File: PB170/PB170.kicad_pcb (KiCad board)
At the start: 4 copper layers, 96.5 x 71.1 mm, 34 parts, among them J1 USB_C_Receptacle_USB2.0-Conne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, J2 USB_B_Micro, Q1 P-MOSFET-MLP_HS, Q2 BC817, SW1 SW_MEC_5E, SW2 SW_MEC_5E, U1 74HC00

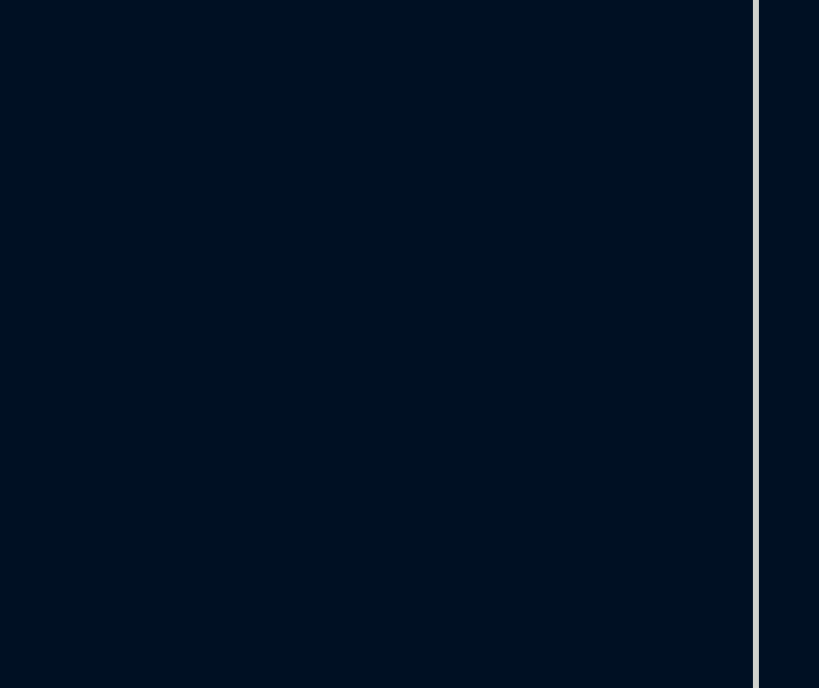
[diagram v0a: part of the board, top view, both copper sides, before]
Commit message: Experimentally added 74HC08 symbol.
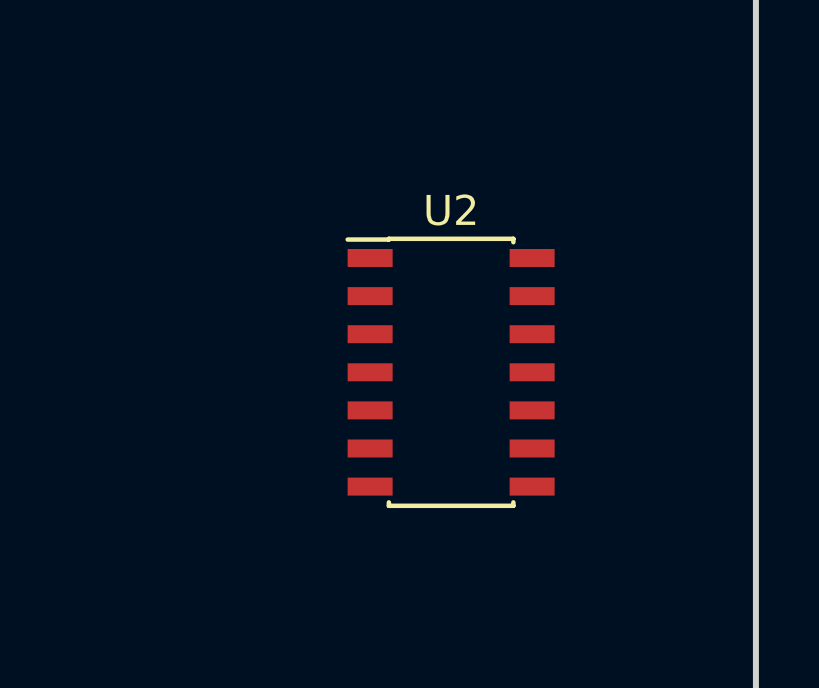
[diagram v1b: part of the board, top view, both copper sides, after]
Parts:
- added U2: 74HC08, Housings_SOIC:SOIC-14_3.9x8.7mm_Pitch1.27mm, F.Cu at (127.0, 48.5)
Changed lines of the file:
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@@
     (tracks 30)
     (zones 0)
-    (modules 34)
-    (nets 32)
+    (modules 35)
+    (nets 44)
   )
   (page A4)
@@
   (net 30 /SheetXOR/IN_B)
   (net 31 OUTPUT)
+  (net 32 "Net-(U2-Pad1)")
+  (net 33 "Net-(U2-Pad2)")
+  (net 34 "Net-(U2-Pad4)")
+  (net 35 "Net-(U2-Pad6)")
+  (net 36 "Net-(U2-Pad8)")
+  (net 37 "Net-(U2-Pad9)")
+  (net 38 "Net-(U2-Pad10)")
+  (net 39 "Net-(U2-Pad11)")
+  (net 40 "Net-(U2-Pad12)")
+  (net 41 "Net-(U2-Pad13)")
+  (net 42 "Net-(U2-Pad3)")
+  (net 43 "Net-(U2-Pad5)")
   (net_class Default "This is the default net class."
     (clearance 0.2)
@@
     (add_net "Net-(U1-Pad13)")
     (add_net "Net-(U1-Pad3)")
+    (add_net "Net-(U2-Pad1)")
+    (add_net "Net-(U2-Pad10)")
+    (add_net "Net-(U2-Pad11)")
+    (add_net "Net-(U2-Pad12)")
+    (add_net "Net-(U2-Pad13)")
+    (add_net "Net-(U2-Pad2)")
+    (add_net "Net-(U2-Pad3)")
+    (add_net "Net-(U2-Pad4)")
+    (add_net "Net-(U2-Pad5)")
+    (add_net "Net-(U2-Pad6)")
+    (add_net "Net-(U2-Pad8)")
+    (add_net "Net-(U2-Pad9)")
     (add_net OUTPUT)
   )
+  (module Housings_SOIC:SOIC-14_3.9x8.7mm_Pitch1.27mm (layer F.Cu)
+    (at 127 48.514)
+    (descr "14-Lead Plastic Small Outline (SL) - Narrow, 3.90 mm Body [SOIC] (see Microchip Packaging Specification 00000049BS.pdf)")
+    (tags "SOIC 1.27")
+    (attr smd)
+    (fp_text reference U2 (at 0 -5.375) (layer F.SilkS)
+      (effects (font (size 1 1) (thickness 0.15)))
+    )
+    (fp_text value 74HC08 (at 0 5.375) (layer F.Fab)
+      (effects (font (size 1 1) (thickness 0.15)))
+    )
+    (fp_line (start -2.075 -4.425) (end -3.45 -4.425) (layer F.SilkS) (width 0.15))
+    (fp_line (start -2.075 4.45) (end 2.075 4.45) (layer F.SilkS) (width 0.15))
+    (fp_line (start -2.075 -4.45) (end 2.075 -4.45) (layer F.SilkS) (width 0.15))
+    (fp_line (start -2.075 4.45) (end -2.075 4.335) (layer F.SilkS) (width 0.15))
+    (fp_line (start 2.075 4.45) (end 2.075 4.335) (layer F.SilkS) (width 0.15))
+    (fp_line (start 2.075 -4.45) (end 2.075 -4.335) (layer F.SilkS) (width 0.15))
+    (fp_line (start -2.075 -4.45) (end -2.075 -4.425) (layer F.SilkS) (width 0.15))
+    (fp_line (start -3.7 4.65) (end 3.7 4.65) (layer F.CrtYd) (width 0.05))
+    (fp_line (start -3.7 -4.65) (end 3.7 -4.65) (layer F.CrtYd) (width 0.05))
+    (fp_line (start 3.7 -4.65) (end 3.7 4.65) (layer F.CrtYd) (width 0.05))
+    (fp_line (start -3.7 -4.65) (end -3.7 4.65) (layer F.CrtYd) (width 0.05))
+    (fp_line (start -1.95 -3.35) (end -0.95 -4.35) (layer F.Fab) (width 0.15))
+    (fp_line (start -1.95 4.35) (end -1.95 -3.35) (layer F.Fab) (width 0.15))
+    (fp_line (start 1.95 4.35) (end -1.95 4.35) (layer F.Fab) (width 0.15))
+    (fp_line (start 1.95 -4.35) (end 1.95 4.35) (layer F.Fab) (width 0.15))
+    (fp_line (start -0.95 -4.35) (end 1.95 -4.35) (layer F.Fab) (width 0.15))
+    (fp_text user %R (at 0 0) (layer F.Fab)
+      (effects (font (size 0.9 0.9) (thickness 0.135)))
+    )
+    (pad 1 smd rect (at -2.7 -3.81) (size 1.5 0.6) (layers F.Cu F.Paste F.Mask)
+      (net 32 "Net-(U2-Pad1)"))
+    (pad 2 smd rect (at -2.7 -2.54) (size 1.5 0.6) (layers F.Cu F.Paste F.Mask)
+      (net 33 "Net-(U2-Pad2)"))
+    (pad 3 smd rect (at -2.7 -1.27) (size 1.5 0.6) (layers F.Cu F.Paste F.Mask)
+      (net 42 "Net-(U2-Pad3)"))
+    (pad 4 smd rect (at -2.7 0) (size 1.5 0.6) (layers F.Cu F.Paste F.Mask)
+      (net 34 "Net-(U2-Pad4)"))
+    (pad 5 smd rect (at -2.7 1.27) (size 1.5 0.6) (layers F.Cu F.Paste F.Mask)
+      (net 43 "Net-(U2-Pad5)"))
+    (pad 6 smd rect (at -2.7 2.54) (size 1.5 0.6) (layers F.Cu F.Paste F.Mask)
+      (net 35 "Net-(U2-Pad6)"))
+    (pad 7 smd rect (at -2.7 3.81) (size 1.5 0.6) (layers F.Cu F.Paste F.Mask)
+      (net 3 GND))
+    (pad 8 smd rect (at 2.7 3.81) (size 1.5 0.6) (layers F.Cu F.Paste F.Mask)
+      (net 36 "Net-(U2-Pad8)"))
+    (pad 9 smd rect (at 2.7 2.54) (size 1.5 0.6) (layers F.Cu F.Paste F.Mask)
+      (net 37 "Net-(U2-Pad9)"))
+    (pad 10 smd rect (at 2.7 1.27) (size 1.5 0.6) (layers F.Cu F.Paste F.Mask)
+      (net 38 "Net-(U2-Pad10)"))
+    (pad 11 smd rect (at 2.7 0) (size 1.5 0.6) (layers F.Cu F.Paste F.Mask)
+      (net 39 "Net-(U2-Pad11)"))
+    (pad 12 smd rect (at 2.7 -1.27) (size 1.5 0.6) (layers F.Cu F.Paste F.Mask)
+      (net 40 "Net-(U2-Pad12)"))
+    (pad 13 smd rect (at 2.7 -2.54) (size 1.5 0.6) (layers F.Cu F.Paste F.Mask)
+      (net 41 "Net-(U2-Pad13)"))
+    (pad 14 smd rect (at 2.7 -3.81) (size 1.5 0.6) (layers F.Cu F.Paste F.Mask)
+      (net 2 +5V))
+    (model ${KISYS3DMOD}/Housings_SOIC.3dshapes/SOIC-14_3.9x8.7mm_Pitch1.27mm.wrl
+      (at (xyz 0 0 0))
+      (scale (xyz 1 1 1))
+      (rotate (xyz 0 0 0))
+    )
+  )
   (module Resistors_SMD:R_0603 (layer F.Cu)

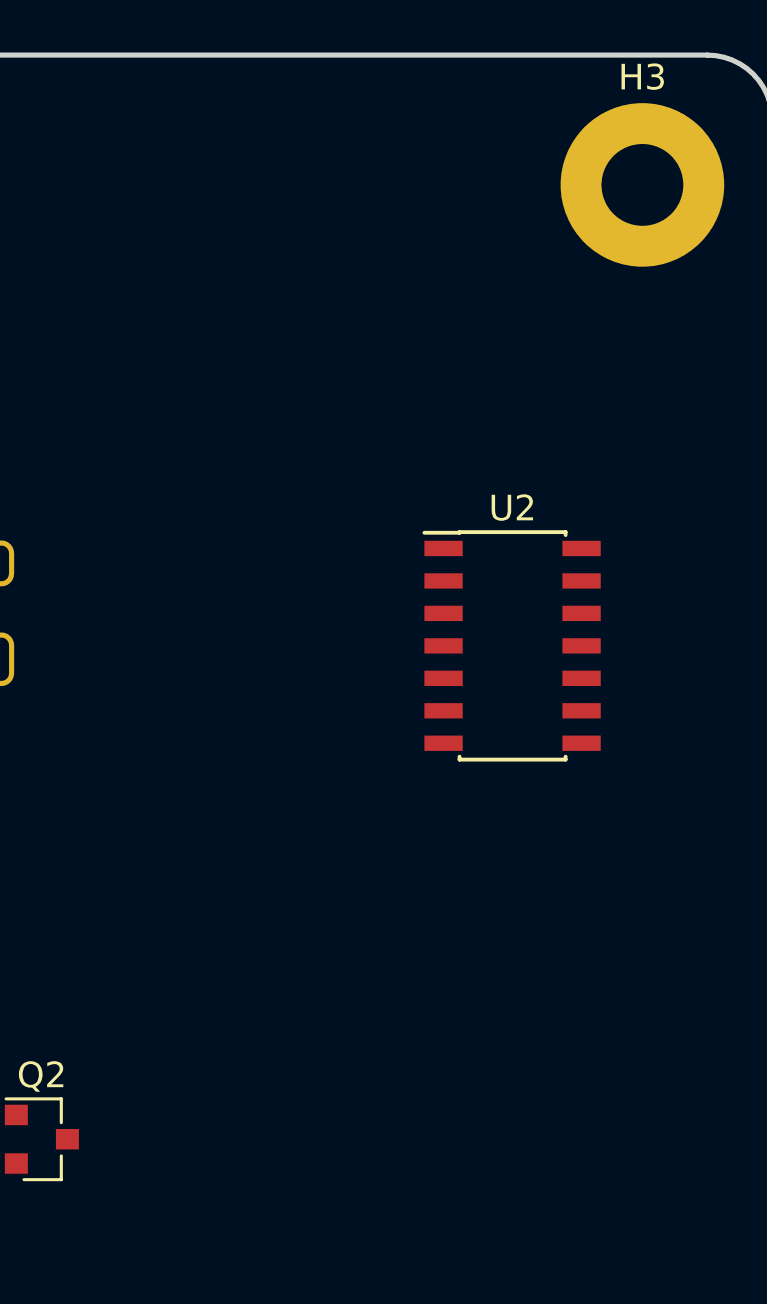
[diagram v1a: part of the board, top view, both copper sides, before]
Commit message: Added 74HC4511D and HEF4518BT.
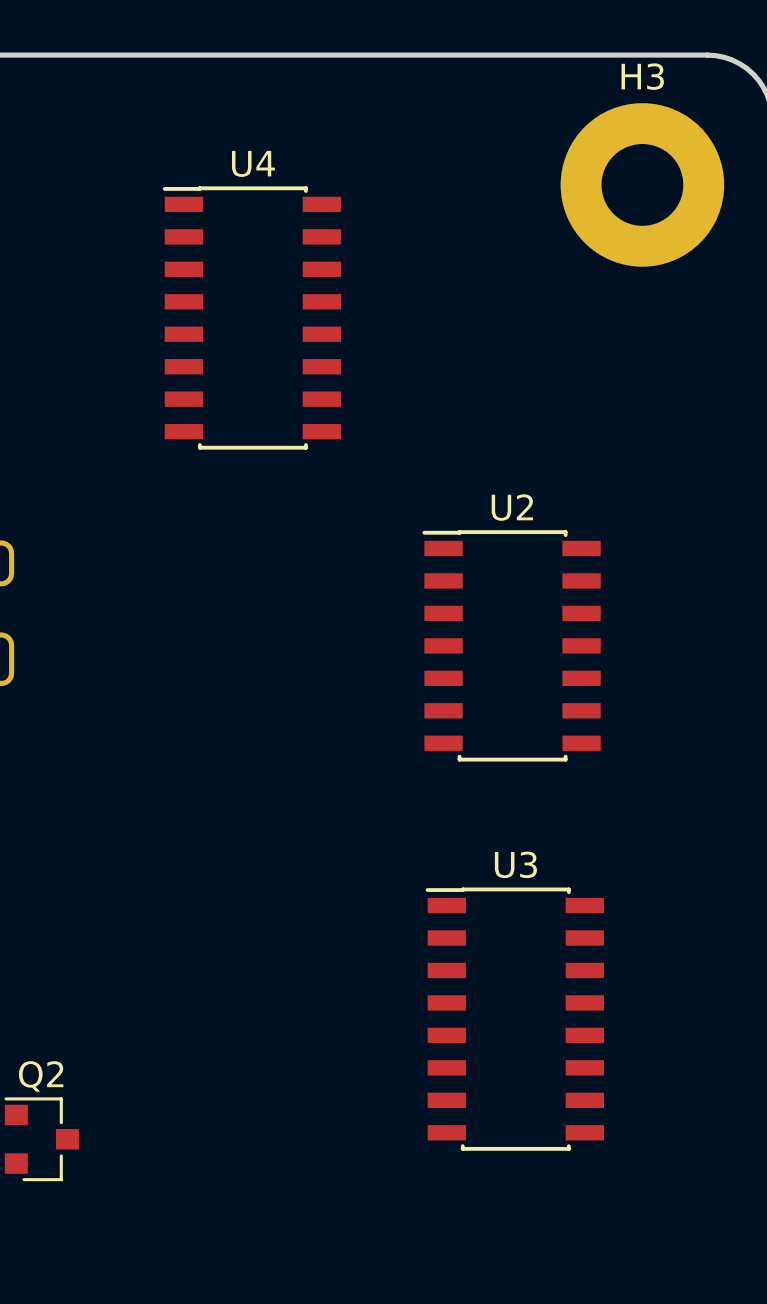
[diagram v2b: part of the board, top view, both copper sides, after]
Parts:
- added U3: 74HC4511D, Housings_SOIC:SOIC-16_3.9x9.9mm_Pitch1.27mm, F.Cu at (127.1, 63.1)
- added U4: HEF4518BT, Housings_SOIC:SOIC-16_3.9x9.9mm_Pitch1.27mm, F.Cu at (116.8, 35.7)
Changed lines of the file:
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@@
     (tracks 30)
     (zones 0)
-    (modules 35)
-    (nets 44)
+    (modules 37)
+    (nets 72)
   )
   (page A4)
@@
   (net 42 "Net-(U2-Pad3)")
   (net 43 "Net-(U2-Pad5)")
+  (net 44 "Net-(U3-Pad1)")
+  (net 45 "Net-(U3-Pad2)")
+  (net 46 "Net-(U3-Pad3)")
+  (net 47 "Net-(U3-Pad4)")
+  (net 48 "Net-(U3-Pad5)")
+  (net 49 "Net-(U3-Pad6)")
+  (net 50 "Net-(U3-Pad7)")
+  (net 51 "Net-(U3-Pad9)")
+  (net 52 "Net-(U3-Pad10)")
+  (net 53 "Net-(U3-Pad11)")
+  (net 54 "Net-(U3-Pad12)")
+  (net 55 "Net-(U3-Pad13)")
+  (net 56 "Net-(U3-Pad14)")
+  (net 57 "Net-(U3-Pad15)")
+  (net 58 "Net-(U4-Pad1)")
+  (net 59 "Net-(U4-Pad2)")
+  (net 60 "Net-(U4-Pad3)")
+  (net 61 "Net-(U4-Pad4)")
+  (net 62 "Net-(U4-Pad5)")
+  (net 63 "Net-(U4-Pad6)")
+  (net 64 "Net-(U4-Pad7)")
+  (net 65 "Net-(U4-Pad9)")
+  (net 66 "Net-(U4-Pad10)")
+  (net 67 "Net-(U4-Pad11)")
+  (net 68 "Net-(U4-Pad12)")
+  (net 69 "Net-(U4-Pad13)")
+  (net 70 "Net-(U4-Pad14)")
+  (net 71 "Net-(U4-Pad15)")
   (net_class Default "This is the default net class."
     (clearance 0.2)
@@
     (add_net "Net-(U2-Pad8)")
     (add_net "Net-(U2-Pad9)")
+    (add_net "Net-(U3-Pad1)")
+    (add_net "Net-(U3-Pad10)")
+    (add_net "Net-(U3-Pad11)")
+    (add_net "Net-(U3-Pad12)")
+    (add_net "Net-(U3-Pad13)")
+    (add_net "Net-(U3-Pad14)")
+    (add_net "Net-(U3-Pad15)")
+    (add_net "Net-(U3-Pad2)")
+    (add_net "Net-(U3-Pad3)")
+    (add_net "Net-(U3-Pad4)")
+    (add_net "Net-(U3-Pad5)")
+    (add_net "Net-(U3-Pad6)")
+    (add_net "Net-(U3-Pad7)")
+    (add_net "Net-(U3-Pad9)")
+    (add_net "Net-(U4-Pad1)")
+    (add_net "Net-(U4-Pad10)")
+    (add_net "Net-(U4-Pad11)")
+    (add_net "Net-(U4-Pad12)")
+    (add_net "Net-(U4-Pad13)")
+    (add_net "Net-(U4-Pad14)")
+    (add_net "Net-(U4-Pad15)")
+    (add_net "Net-(U4-Pad2)")
+    (add_net "Net-(U4-Pad3)")
+    (add_net "Net-(U4-Pad4)")
+    (add_net "Net-(U4-Pad5)")
+    (add_net "Net-(U4-Pad6)")
+    (add_net "Net-(U4-Pad7)")
+    (add_net "Net-(U4-Pad9)")
     (add_net OUTPUT)
   )
+  (module Housings_SOIC:SOIC-16_3.9x9.9mm_Pitch1.27mm (layer F.Cu)
+    (at 116.84 35.687)
+    (descr "16-Lead Plastic Small Outline (SL) - Narrow, 3.90 mm Body [SOIC] (see Microchip Packaging Specification 00000049BS.pdf)")
+    (tags "SOIC 1.27")
+    (attr smd)
+    (fp_text reference U4 (at 0 -6) (layer F.SilkS)
+      (effects (font (size 1 1) (thickness 0.15)))
+    )
+    (fp_text value HEF4518BT (at 0 6) (layer F.Fab)
+      (effects (font (size 1 1) (thickness 0.15)))
+    )
+    (fp_line (start -2.075 -5.05) (end -3.45 -5.05) (layer F.SilkS) (width 0.15))
+    (fp_line (start -2.075 5.075) (end 2.075 5.075) (layer F.SilkS) (width 0.15))
+    (fp_line (start -2.075 -5.075) (end 2.075 -5.075) (layer F.SilkS) (width 0.15))
+    (fp_line (start -2.075 5.075) (end -2.075 4.97) (layer F.SilkS) (width 0.15))
+    (fp_line (start 2.075 5.075) (end 2.075 4.97) (layer F.SilkS) (width 0.15))
+    (fp_line (start 2.075 -5.075) (end 2.075 -4.97) (layer F.SilkS) (width 0.15))
+    (fp_line (start -2.075 -5.075) (end -2.075 -5.05) (layer F.SilkS) (width 0.15))
+    (fp_line (start -3.7 5.25) (end 3.7 5.25) (layer F.CrtYd) (width 0.05))
+    (fp_line (start -3.7 -5.25) (end 3.7 -5.25) (layer F.CrtYd) (width 0.05))
+    (fp_line (start 3.7 -5.25) (end 3.7 5.25) (layer F.CrtYd) (width 0.05))
+    (fp_line (start -3.7 -5.25) (end -3.7 5.25) (layer F.CrtYd) (width 0.05))
+    (fp_line (start -1.95 -3.95) (end -0.95 -4.95) (layer F.Fab) (width 0.15))
+    (fp_line (start -1.95 4.95) (end -1.95 -3.95) (layer F.Fab) (width 0.15))
+    (fp_line (start 1.95 4.95) (end -1.95 4.95) (layer F.Fab) (width 0.15))
+    (fp_line (start 1.95 -4.95) (end 1.95 4.95) (layer F.Fab) (width 0.15))
+    (fp_line (start -0.95 -4.95) (end 1.95 -4.95) (layer F.Fab) (width 0.15))
+    (fp_text user %R (at 0 0) (layer F.Fab)
+      (effects (font (size 0.9 0.9) (thickness 0.135)))
+    )
+    (pad 1 smd rect (at -2.7 -4.445) (size 1.5 0.6) (layers F.Cu F.Paste F.Mask)
+      (net 58 "Net-(U4-Pad1)"))
+    (pad 2 smd rect (at -2.7 -3.175) (size 1.5 0.6) (layers F.Cu F.Paste F.Mask)
+      (net 59 "Net-(U4-Pad2)"))
+    (pad 3 smd rect (at -2.7 -1.905) (size 1.5 0.6) (layers F.Cu F.Paste F.Mask)
+      (net 60 "Net-(U4-Pad3)"))
+    (pad 4 smd rect (at -2.7 -0.635) (size 1.5 0.6) (layers F.Cu F.Paste F.Mask)
+      (net 61 "Net-(U4-Pad4)"))
+    (pad 5 smd rect (at -2.7 0.635) (size 1.5 0.6) (layers F.Cu F.Paste F.Mask)
+      (net 62 "Net-(U4-Pad5)"))
+    (pad 6 smd rect (at -2.7 1.905) (size 1.5 0.6) (layers F.Cu F.Paste F.Mask)
+      (net 63 "Net-(U4-Pad6)"))
+    (pad 7 smd rect (at -2.7 3.175) (size 1.5 0.6) (layers F.Cu F.Paste F.Mask)
+      (net 64 "Net-(U4-Pad7)"))
+    (pad 8 smd rect (at -2.7 4.445) (size 1.5 0.6) (layers F.Cu F.Paste F.Mask)
+      (net 3 GND))
+    (pad 9 smd rect (at 2.7 4.445) (size 1.5 0.6) (layers F.Cu F.Paste F.Mask)
+      (net 65 "Net-(U4-Pad9)"))
+    (pad 10 smd rect (at 2.7 3.175) (size 1.5 0.6) (layers F.Cu F.Paste F.Mask)
+      (net 66 "Net-(U4-Pad10)"))
+    (pad 11 smd rect (at 2.7 1.905) (size 1.5 0.6) (layers F.Cu F.Paste F.Mask)
+      (net 67 "Net-(U4-Pad11)"))
+    (pad 12 smd rect (at 2.7 0.635) (size 1.5 0.6) (layers F.Cu F.Paste F.Mask)
+      (net 68 "Net-(U4-Pad12)"))
+    (pad 13 smd rect (at 2.7 -0.635) (size 1.5 0.6) (layers F.Cu F.Paste F.Mask)
+      (net 69 "Net-(U4-Pad13)"))
+    (pad 14 smd rect (at 2.7 -1.905) (size 1.5 0.6) (layers F.Cu F.Paste F.Mask)
+      (net 70 "Net-(U4-Pad14)"))
+    (pad 15 smd rect (at 2.7 -3.175) (size 1.5 0.6) (layers F.Cu F.Paste F.Mask)
+      (net 71 "Net-(U4-Pad15)"))
+    (pad 16 smd rect (at 2.7 -4.445) (size 1.5 0.6) (layers F.Cu F.Paste F.Mask)
+      (net 2 +5V))
+    (model ${KISYS3DMOD}/Housings_SOIC.3dshapes/SOIC-16_3.9x9.9mm_Pitch1.27mm.wrl
+      (at (xyz 0 0 0))
+      (scale (xyz 1 1 1))
+      (rotate (xyz 0 0 0))
+    )
+  )
+  (module Housings_SOIC:SOIC-16_3.9x9.9mm_Pitch1.27mm (layer F.Cu)
+    (at 127.127 63.119)
+    (descr "16-Lead Plastic Small Outline (SL) - Narrow, 3.90 mm Body [SOIC] (see Microchip Packaging Specification 00000049BS.pdf)")
+    (tags "SOIC 1.27")
+    (attr smd)
+    (fp_text reference U3 (at 0 -6) (layer F.SilkS)
+      (effects (font (size 1 1) (thickness 0.15)))
+    )
+    (fp_text value 74HC4511D (at 0 6) (layer F.Fab)
+      (effects (font (size 1 1) (thickness 0.15)))
+    )
+    (fp_line (start -0.95 -4.95) (end 1.95 -4.95) (layer F.Fab) (width 0.15))
+    (fp_line (start 1.95 -4.95) (end 1.95 4.95) (layer F.Fab) (width 0.15))
+    (fp_line (start 1.95 4.95) (end -1.95 4.95) (layer F.Fab) (width 0.15))
+    (fp_line (start -1.95 4.95) (end -1.95 -3.95) (layer F.Fab) (width 0.15))
+    (fp_line (start -1.95 -3.95) (end -0.95 -4.95) (layer F.Fab) (width 0.15))
+    (fp_line (start -3.7 -5.25) (end -3.7 5.25) (layer F.CrtYd) (width 0.05))
+    (fp_line (start 3.7 -5.25) (end 3.7 5.25) (layer F.CrtYd) (width 0.05))
+    (fp_line (start -3.7 -5.25) (end 3.7 -5.25) (layer F.CrtYd) (width 0.05))
+    (fp_line (start -3.7 5.25) (end 3.7 5.25) (layer F.CrtYd) (width 0.05))
+    (fp_line (start -2.075 -5.075) (end -2.075 -5.05) (layer F.SilkS) (width 0.15))
+    (fp_line (start 2.075 -5.075) (end 2.075 -4.97) (layer F.SilkS) (width 0.15))
+    (fp_line (start 2.075 5.075) (end 2.075 4.97) (layer F.SilkS) (width 0.15))
+    (fp_line (start -2.075 5.075) (end -2.075 4.97) (layer F.SilkS) (width 0.15))
+    (fp_line (start -2.075 -5.075) (end 2.075 -5.075) (layer F.SilkS) (width 0.15))
+    (fp_line (start -2.075 5.075) (end 2.075 5.075) (layer F.SilkS) (width 0.15))
+    (fp_line (start -2.075 -5.05) (end -3.45 -5.05) (layer F.SilkS) (width 0.15))
+    (fp_text user %R (at 0 0) (layer F.Fab)
+      (effects (font (size 0.9 0.9) (thickness 0.135)))
+    )
+    (pad 1 smd rect (at -2.7 -4.445) (size 1.5 0.6) (layers F.Cu F.Paste F.Mask)
+      (net 44 "Net-(U3-Pad1)"))
+    (pad 2 smd rect (at -2.7 -3.175) (size 1.5 0.6) (layers F.Cu F.Paste F.Mask)
+      (net 45 "Net-(U3-Pad2)"))
+    (pad 3 smd rect (at -2.7 -1.905) (size 1.5 0.6) (layers F.Cu F.Paste F.Mask)
+      (net 46 "Net-(U3-Pad3)"))
+    (pad 4 smd rect (at -2.7 -0.635) (size 1.5 0.6) (layers F.Cu F.Paste F.Mask)
+      (net 47 "Net-(U3-Pad4)"))
+    (pad 5 smd rect (at -2.7 0.635) (size 1.5 0.6) (layers F.Cu F.Paste F.Mask)
+      (net 48 "Net-(U3-Pad5)"))
+    (pad 6 smd rect (at -2.7 1.905) (size 1.5 0.6) (layers F.Cu F.Paste F.Mask)
+      (net 49 "Net-(U3-Pad6)"))
+    (pad 7 smd rect (at -2.7 3.175) (size 1.5 0.6) (layers F.Cu F.Paste F.Mask)
+      (net 50 "Net-(U3-Pad7)"))
+    (pad 8 smd rect (at -2.7 4.445) (size 1.5 0.6) (layers F.Cu F.Paste F.Mask)
+      (net 3 GND))
+    (pad 9 smd rect (at 2.7 4.445) (size 1.5 0.6) (layers F.Cu F.Paste F.Mask)
+      (net 51 "Net-(U3-Pad9)"))
+    (pad 10 smd rect (at 2.7 3.175) (size 1.5 0.6) (layers F.Cu F.Paste F.Mask)
+      (net 52 "Net-(U3-Pad10)"))
+    (pad 11 smd rect (at 2.7 1.905) (size 1.5 0.6) (layers F.Cu F.Paste F.Mask)
+      (net 53 "Net-(U3-Pad11)"))
+    (pad 12 smd rect (at 2.7 0.635) (size 1.5 0.6) (layers F.Cu F.Paste F.Mask)
+      (net 54 "Net-(U3-Pad12)"))
+    (pad 13 smd rect (at 2.7 -0.635) (size 1.5 0.6) (layers F.Cu F.Paste F.Mask)
+      (net 55 "Net-(U3-Pad13)"))
+    (pad 14 smd rect (at 2.7 -1.905) (size 1.5 0.6) (layers F.Cu F.Paste F.Mask)
+      (net 56 "Net-(U3-Pad14)"))
+    (pad 15 smd rect (at 2.7 -3.175) (size 1.5 0.6) (layers F.Cu F.Paste F.Mask)
+      (net 57 "Net-(U3-Pad15)"))
+    (pad 16 smd rect (at 2.7 -4.445) (size 1.5 0.6) (layers F.Cu F.Paste F.Mask)
+      (net 2 +5V))
+    (model ${KISYS3DMOD}/Housings_SOIC.3dshapes/SOIC-16_3.9x9.9mm_Pitch1.27mm.wrl
+      (at (xyz 0 0 0))
+      (scale (xyz 1 1 1))
+      (rotate (xyz 0 0 0))
+    )
+  )
   (module Housings_SOIC:SOIC-14_3.9x8.7mm_Pitch1.27mm (layer F.Cu)
